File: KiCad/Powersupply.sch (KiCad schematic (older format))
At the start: 11 parts, among them J501 TE_Connectivity_282834-3, J502 CONN_01X03_FEMALE, U501 LM1086-5V, U502 LM1086-3.3V

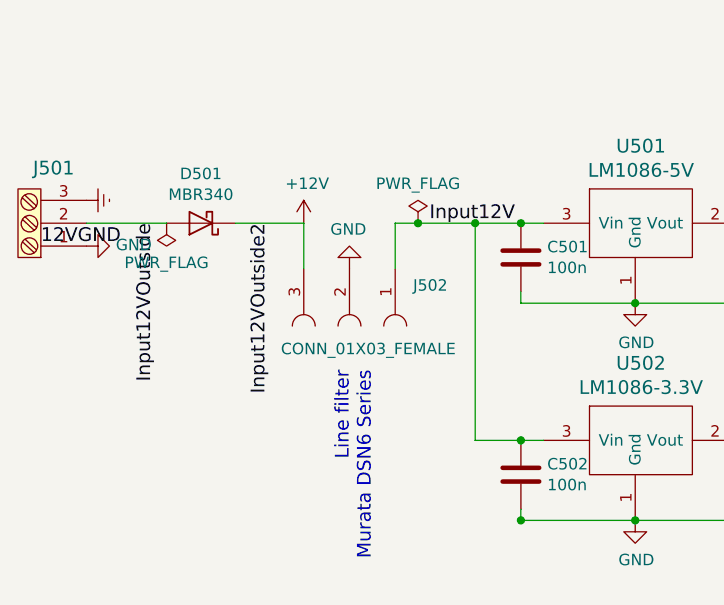
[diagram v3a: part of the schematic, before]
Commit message: Halfway through routing - need better layout to prevent rats nest
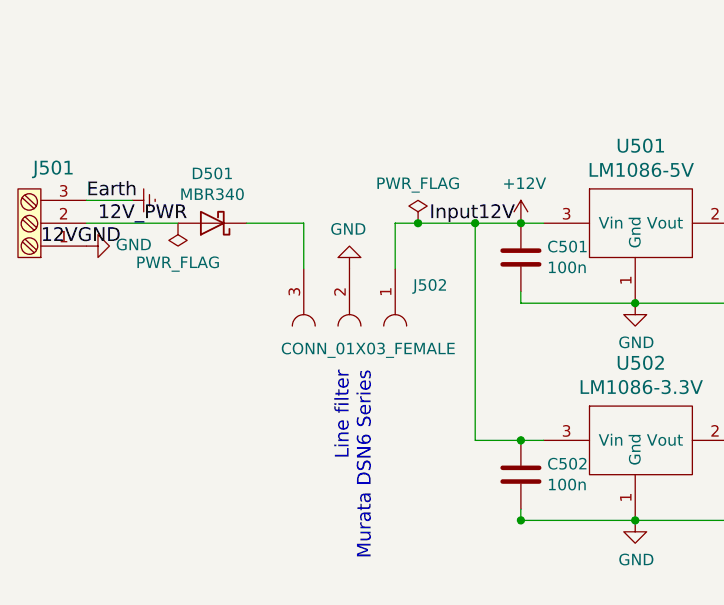
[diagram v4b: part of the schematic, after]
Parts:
- C505, C506: footprint Capacitors_THT:CP_Radial_D7.5mm_P2.50mm -> Capacitors_THT:CP_Radial_D6.3mm_P2.50mm
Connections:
- net labels added: 12V_PWR
- net labels removed: Input12VOutside, Input12VOutside2
- wire segments 27 -> 28
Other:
- moved on the sheet: D501
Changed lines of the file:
@@
 POWER3V3
 $Comp
-L +3V3 #PWR0104
+L +3V3 #PWR0112
 U 1 1 592AD7CB
 P 2200 1500
-F 0 "#PWR0104" H 2200 1350 50  0001 C CNN
+F 0 "#PWR0112" H 2200 1350 50  0001 C CNN
 F 1 "+3V3" V 2215 1628 50  0000 L CNN
 F 2 "" H 2200 1500 50  0001 C CNN
@@
 	2100 1500 2200 1500
 $Comp
-L PWR_FLAG #FLG0105
+L PWR_FLAG #FLG0113
 U 1 1 592B4E13
 P 2850 1450
-F 0 "#FLG0105" H 2850 1525 50  0001 C CNN
+F 0 "#FLG0113" H 2850 1525 50  0001 C CNN
 F 1 "PWR_FLAG" H 2850 1624 50  0000 C CNN
 F 2 "" H 2850 1450 50  0001 C CNN
@@
 $EndComp
 $Comp
-L GND #PWR0106
+L GND #PWR0114
 U 1 1 592B4E96
 P 2850 1450
-F 0 "#PWR0106" H 2850 1200 50  0001 C CNN
+F 0 "#PWR0114" H 2850 1200 50  0001 C CNN
 F 1 "GND" H 2855 1277 50  0000 C CNN
 F 2 "" H 2850 1450 50  0001 C CNN
@@
 $EndComp
 $Comp
-L GND #PWR0107
+L GND #PWR0115
 U 1 1 5924C039
 P 3350 4250
-F 0 "#PWR0107" H 3350 4000 50  0001 C CNN
+F 0 "#PWR0115" H 3350 4000 50  0001 C CNN
 F 1 "GND" H 3355 4077 50  0000 C CNN
 F 2 "" H 3350 4250 50  0001 C CNN
@@
 F 0 "C506" H 4768 4096 50  0000 L CNN
 F 1 "100uF" H 4768 4005 50  0000 L CNN
-F 2 "Capacitors_THT:CP_Radial_D7.5mm_P2.50mm" H 4688 3900 50  0001 C CNN
-F 3 "http://se.rs-online.com/web/p/aluminium-capacitors/8650656/" H 4650 4050 50  0001 C CNN
+F 2 "Capacitors_THT:CP_Radial_D6.3mm_P2.50mm" H 4688 3900 50  0001 C CNN
+F 3 "https://www.digikey.se/product-detail/en/nichicon/ULD1C101MED1TD/493-14722-1-ND/6161730" H 4650 4050 50  0001 C CNN
 	1    4650 4050
 	1    0    0    -1
@@
 Connection ~ 4200 2950
 $Comp
-L GND #PWR0108
+L GND #PWR0116
 U 1 1 5924DE85
 P 950 3050
-F 0 "#PWR0108" H 950 2800 50  0001 C CNN
+F 0 "#PWR0116" H 950 2800 50  0001 C CNN
 F 1 "GND" V 955 2922 50  0000 R CNN
 F 2 "" H 950 3050 50  0001 C CNN
@@
 $EndComp
 $Comp
-L PWR_FLAG #FLG0109
+L PWR_FLAG #FLG0117
 U 1 1 5924DE8B
-P 1300 2950
-F 0 "#FLG0109" H 1300 3025 50  0001 C CNN
-F 1 "PWR_FLAG" H 1300 3123 50  0000 C CNN
-F 2 "" H 1300 2950 50  0001 C CNN
-F 3 "" H 1300 2950 50  0001 C CNN
-	1    1300 2950
+P 1350 2950
+F 0 "#FLG0117" H 1350 3025 50  0001 C CNN
+F 1 "PWR_FLAG" H 1350 3123 50  0000 C CNN
+F 2 "" H 1350 2950 50  0001 C CNN
+F 3 "" H 1350 2950 50  0001 C CNN
+	1    1350 2950
 	-1   0    0    1
 $EndComp
@@
 	2050 1850 2200 1850
 $Comp
-L +5V #PWR0110
+L +5V #PWR0118
 U 1 1 5924EF19
 P 2200 1850
-F 0 "#PWR0110" H 2200 1700 50  0001 C CNN
+F 0 "#PWR0118" H 2200 1700 50  0001 C CNN
 F 1 "+5V" V 2215 1978 50  0000 L CNN
 F 2 "" H 2200 1850 50  0001 C CNN
@@
 F 0 "C505" H 4768 3146 50  0000 L CNN
 F 1 "100uF" H 4768 3055 50  0000 L CNN
-F 2 "Capacitors_THT:CP_Radial_D7.5mm_P2.50mm" H 4688 2950 50  0001 C CNN
-F 3 "http://se.rs-online.com/web/p/aluminium-capacitors/8650656/" H 4650 3100 50  0001 C CNN
+F 2 "Capacitors_THT:CP_Radial_D6.3mm_P2.50mm" H 4688 2950 50  0001 C CNN
+F 3 "https://www.digikey.se/product-detail/en/nichicon/ULD1C101MED1TD/493-14722-1-ND/6161730" H 4650 3100 50  0001 C CNN
 	1    4650 3100
 	1    0    0    -1
@@
 $EndComp
 $Comp
-L GND #PWR0111
+L GND #PWR0119
 U 1 1 5924DE5E
 P 3350 3300
-F 0 "#PWR0111" H 3350 3050 50  0001 C CNN
+F 0 "#PWR0119" H 3350 3050 50  0001 C CNN
 F 1 "GND" H 3355 3127 50  0000 C CNN
 F 2 "" H 3350 3300 50  0001 C CNN
@@
 L MBR340 D501
 U 1 1 5928EED5
-P 1450 2950
-F 0 "D501" H 1450 2734 50  0000 C CNN
-F 1 "MBR340" H 1450 2825 50  0000 C CNN
-F 2 "Diodes_SMD:D_SMB" H 1450 2775 50  0001 C CNN
-F 3 "" H 1450 2950 50  0001 C CNN
-	1    1450 2950
-	-1   0    0    1
-$EndComp
-Text Label 1250 2950 3    60   ~ 0
-Input12VOutside
-Wire Wire Line
-	950  2950 1300 2950
+P 1500 2950
+F 0 "D501" H 1500 2734 50  0000 C CNN
+F 1 "MBR340" H 1500 2825 50  0000 C CNN
+F 2 "Diodes_SMD:D_SMB" H 1500 2775 50  0001 C CNN
+F 3 "" H 1500 2950 50  0001 C CNN
+	1    1500 2950
+	-1   0    0    1
+$EndComp
+Wire Wire Line
+	950  2950 1350 2950
 $Comp
 L CONN_01X03_FEMALE J502
@@
 $EndComp
 $Comp
-L GND #PWR0112
+L GND #PWR0120
 U 1 1 592909E6
 P 2100 3150
-F 0 "#PWR0112" H 2100 2900 50  0001 C CNN
+F 0 "#PWR0120" H 2100 2900 50  0001 C CNN
 F 1 "GND" H 2105 2977 50  0000 C CNN
 F 2 "" H 2100 3150 50  0001 C CNN
@@
 	-1   0    0    1
 $EndComp
-Text Label 1750 2950 3    60   ~ 0
-Input12VOutside2
-Wire Wire Line
-	1600 2950 1900 2950
+Wire Wire Line
+	1650 2950 1900 2950
 Wire Wire Line
 	1900 2950 1900 3150
 $Comp
-L +12V #PWR0113
+L +12V #PWR0121
 U 1 1 592CA1C3
-P 1900 2950
-F 0 "#PWR0113" H 1900 2800 50  0001 C CNN
-F 1 "+12V" H 1915 3123 50  0000 C CNN
-F 2 "" H 1900 2950 50  0001 C CNN
-F 3 "" H 1900 2950 50  0001 C CNN
-	1    1900 2950
+P 2850 2950
+F 0 "#PWR0121" H 2850 2800 50  0001 C CNN
+F 1 "+12V" H 2865 3123 50  0000 C CNN
+F 2 "" H 2850 2950 50  0001 C CNN
+F 3 "" H 2850 2950 50  0001 C CNN
+	1    2850 2950
 	1    0    0    -1
 $EndComp
@@
 Connection ~ 4200 4250
 $Comp
-L PWR_FLAG #FLG0114
+L PWR_FLAG #FLG0122
 U 1 1 592E87DD
 P 3450 1450
-F 0 "#FLG0114" H 3450 1525 50  0001 C CNN
+F 0 "#FLG0122" H 3450 1525 50  0001 C CNN
 F 1 "PWR_FLAG" H 3450 1623 50  0000 C CNN
 F 2 "" H 3450 1450 50  0001 C CNN
@@
 $EndComp
 $Comp
-L +12V #PWR0115
+L +12V #PWR0123
 U 1 1 592E8840
 P 3450 1450
-F 0 "#PWR0115" H 3450 1300 50  0001 C CNN
+F 0 "#PWR0123" H 3450 1300 50  0001 C CNN
 F 1 "+12V" H 3465 1623 50  0000 C CNN
 F 2 "" H 3450 1450 50  0001 C CNN
@@
 $EndComp
 $Comp
-L PWR_FLAG #FLG0116
+L PWR_FLAG #FLG0124
 U 1 1 592EF7D9
 P 2400 2950
-F 0 "#FLG0116" H 2400 3025 50  0001 C CNN
+F 0 "#FLG0124" H 2400 3025 50  0001 C CNN
 F 1 "PWR_FLAG" H 2400 3123 50  0000 C CNN
 F 2 "" H 2400 2950 50  0001 C CNN
@@
 Connection ~ 2400 2950
 $Comp
-L Earth #PWR0117
+L Earth #PWR0125
 U 1 1 5933481E
-P 950 2850
-F 0 "#PWR0117" H 950 2600 50  0001 C CNN
-F 1 "Earth" H 950 2700 50  0001 C CNN
-F 2 "" H 950 2850 50  0001 C CNN
-F 3 "" H 950 2850 50  0001 C CNN
-	1    950  2850
+P 1150 2850
+F 0 "#PWR0125" H 1150 2600 50  0001 C CNN
+F 1 "Earth" H 1150 2700 50  0001 C CNN
+F 2 "" H 1150 2850 50  0001 C CNN
+F 3 "" H 1150 2850 50  0001 C CNN
+	1    1150 2850
 	0    -1   -1   0
 $EndComp
@@
 $EndComp
 $Comp
-L Earth #PWR0118
+L Earth #PWR0126
 U 1 1 59344C28
 P 3150 1500
-F 0 "#PWR0118" H 3150 1250 50  0001 C CNN
+F 0 "#PWR0126" H 3150 1250 50  0001 C CNN
 F 1 "Earth" H 3150 1350 50  0001 C CNN
 F 2 "" H 3150 1500 50  0001 C CNN
@@
 Wire Wire Line
 	3150 1450 2850 1450
+Wire Wire Line
+	950  2850 1150 2850
+Text Label 950  2850 0    60   ~ 0
+Earth
+Text Label 1000 2950 0    60   ~ 0
+12V_PWR
 $EndSCHEMATC

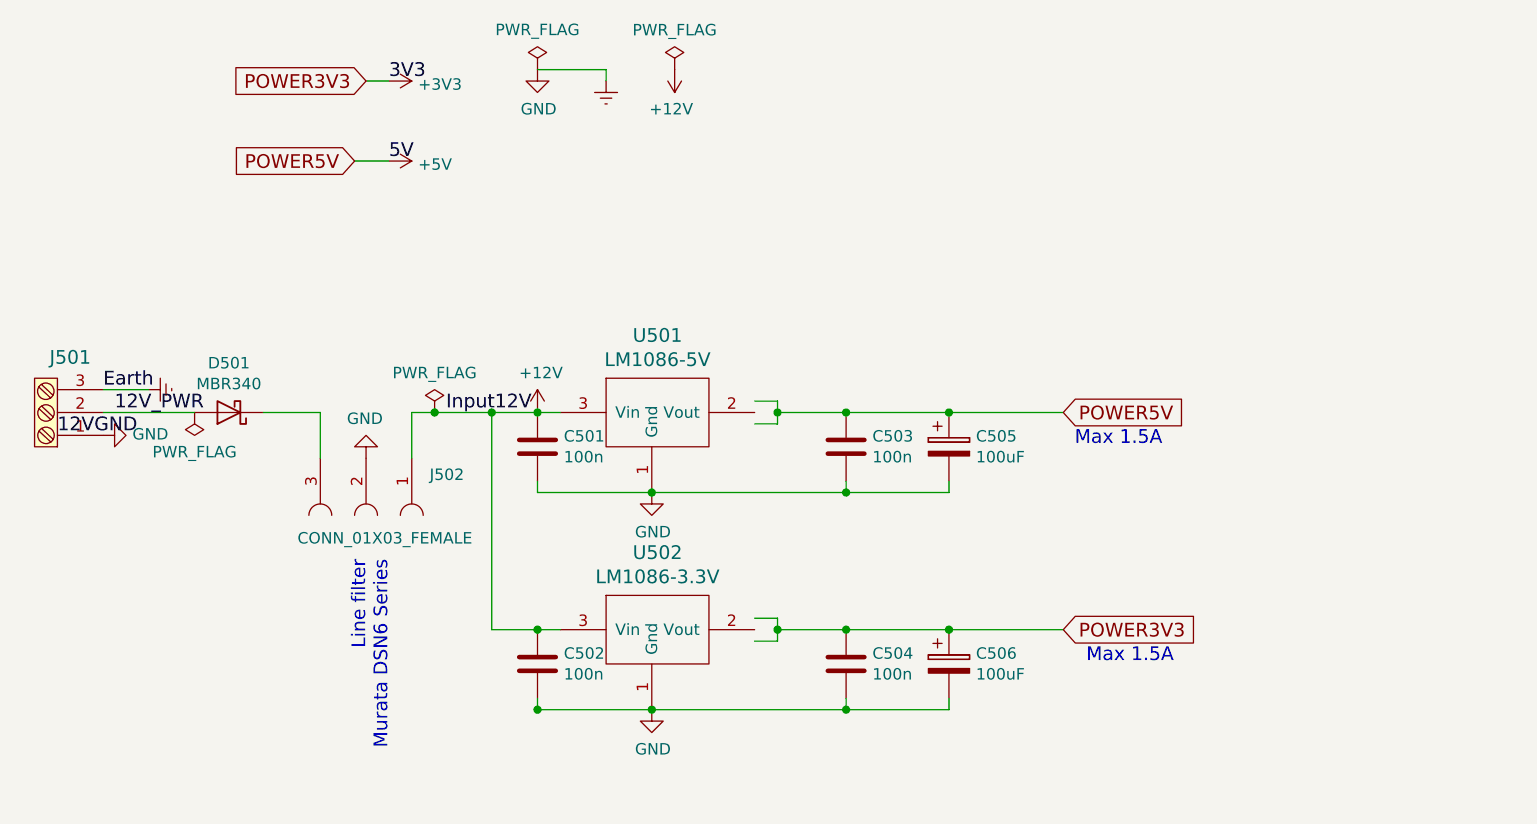
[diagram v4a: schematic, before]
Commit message: New sense input circuits. New layout
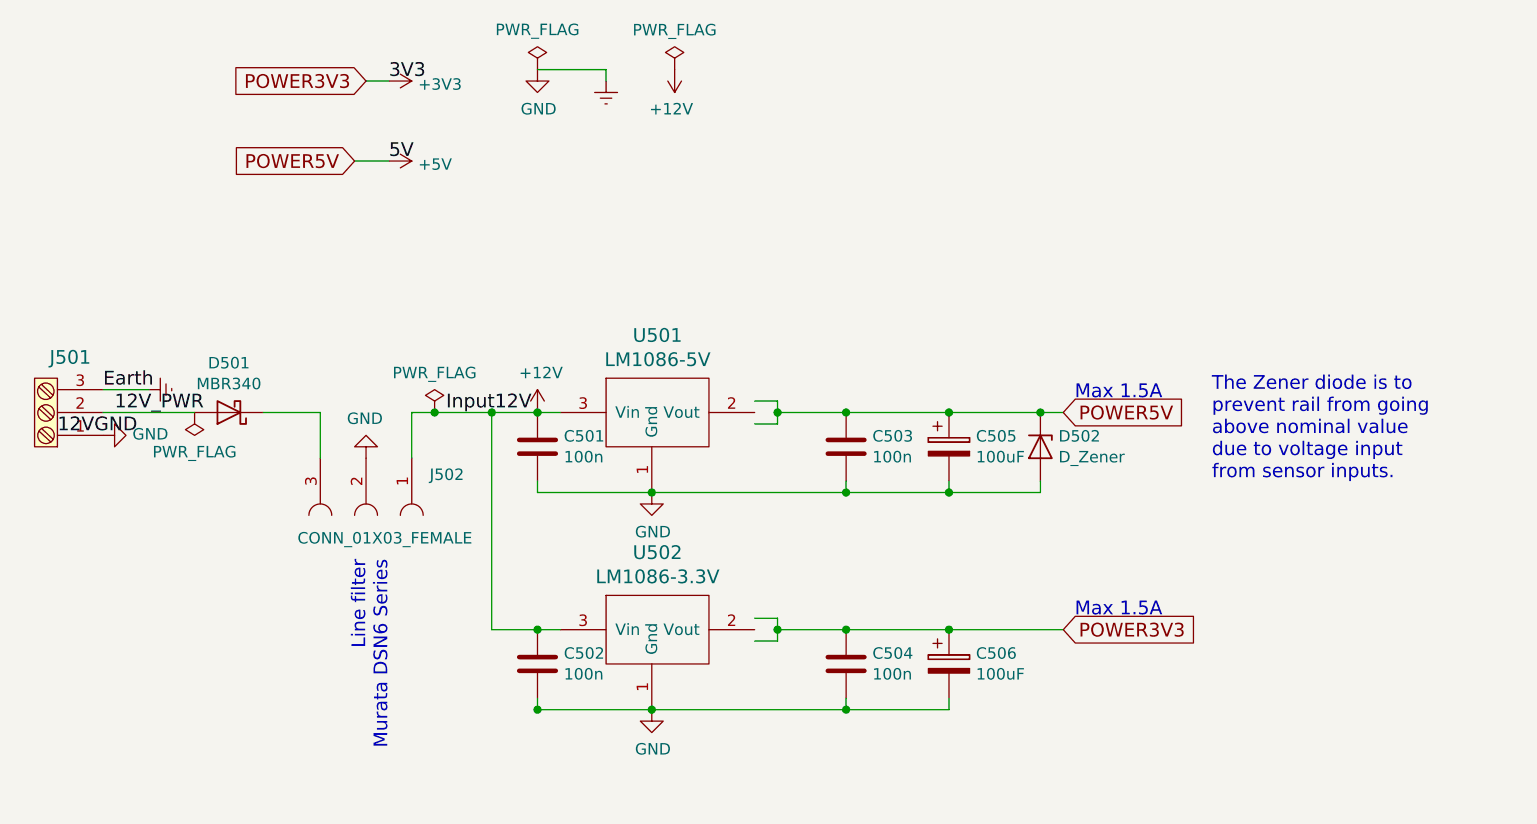
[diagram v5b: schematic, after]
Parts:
- added D502: D_Zener, Diodes_SMD:D_SOD-123, symbol D_Zener
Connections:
- wire segments 28 -> 29
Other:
- note added: "The Zener diode is to\nprevent rail from going\nabove nominal value\ndue to voltage input\nfrom sensor inputs."
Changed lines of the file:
@@
 POWER3V3
 $Comp
-L +3V3 #PWR0112
+L +3V3 #PWR0120
 U 1 1 592AD7CB
 P 2200 1500
-F 0 "#PWR0112" H 2200 1350 50  0001 C CNN
+F 0 "#PWR0120" H 2200 1350 50  0001 C CNN
 F 1 "+3V3" V 2215 1628 50  0000 L CNN
 F 2 "" H 2200 1500 50  0001 C CNN
@@
 	2100 1500 2200 1500
 $Comp
-L PWR_FLAG #FLG0113
+L PWR_FLAG #FLG0121
 U 1 1 592B4E13
 P 2850 1450
-F 0 "#FLG0113" H 2850 1525 50  0001 C CNN
+F 0 "#FLG0121" H 2850 1525 50  0001 C CNN
 F 1 "PWR_FLAG" H 2850 1624 50  0000 C CNN
 F 2 "" H 2850 1450 50  0001 C CNN
@@
 $EndComp
 $Comp
-L GND #PWR0114
+L GND #PWR0122
 U 1 1 592B4E96
 P 2850 1450
-F 0 "#PWR0114" H 2850 1200 50  0001 C CNN
+F 0 "#PWR0122" H 2850 1200 50  0001 C CNN
 F 1 "GND" H 2855 1277 50  0000 C CNN
 F 2 "" H 2850 1450 50  0001 C CNN
@@
 $EndComp
 $Comp
-L GND #PWR0115
+L GND #PWR0123
 U 1 1 5924C039
 P 3350 4250
-F 0 "#PWR0115" H 3350 4000 50  0001 C CNN
+F 0 "#PWR0123" H 3350 4000 50  0001 C CNN
 F 1 "GND" H 3355 4077 50  0000 C CNN
 F 2 "" H 3350 4250 50  0001 C CNN
@@
 Connection ~ 4200 2950
 $Comp
-L GND #PWR0116
+L GND #PWR0124
 U 1 1 5924DE85
 P 950 3050
-F 0 "#PWR0116" H 950 2800 50  0001 C CNN
+F 0 "#PWR0124" H 950 2800 50  0001 C CNN
 F 1 "GND" V 955 2922 50  0000 R CNN
 F 2 "" H 950 3050 50  0001 C CNN
@@
 $EndComp
 $Comp
-L PWR_FLAG #FLG0117
+L PWR_FLAG #FLG0125
 U 1 1 5924DE8B
 P 1350 2950
-F 0 "#FLG0117" H 1350 3025 50  0001 C CNN
+F 0 "#FLG0125" H 1350 3025 50  0001 C CNN
 F 1 "PWR_FLAG" H 1350 3123 50  0000 C CNN
 F 2 "" H 1350 2950 50  0001 C CNN
@@
 	2050 1850 2200 1850
 $Comp
-L +5V #PWR0118
+L +5V #PWR0126
 U 1 1 5924EF19
 P 2200 1850
-F 0 "#PWR0118" H 2200 1700 50  0001 C CNN
+F 0 "#PWR0126" H 2200 1700 50  0001 C CNN
 F 1 "+5V" V 2215 1978 50  0000 L CNN
 F 2 "" H 2200 1850 50  0001 C CNN
@@
 	1    0    0    -1
 $EndComp
-Text Notes 5200 3100 0    60   ~ 0
+Text Notes 5200 2900 0    60   ~ 0
 Max 1.5A
-Text Notes 5250 4050 0    60   ~ 0
+Text Notes 5200 3850 0    60   ~ 0
 Max 1.5A
 Text Label 2450 2950 0    60   ~ 0
@@
 $EndComp
 $Comp
-L GND #PWR0119
+L GND #PWR0127
 U 1 1 5924DE5E
 P 3350 3300
-F 0 "#PWR0119" H 3350 3050 50  0001 C CNN
+F 0 "#PWR0127" H 3350 3050 50  0001 C CNN
 F 1 "GND" H 3355 3127 50  0000 C CNN
 F 2 "" H 3350 3300 50  0001 C CNN
@@
 $EndComp
 Wire Wire Line
-	2850 3300 4650 3300
+	2850 3300 5050 3300
 Wire Wire Line
 	2850 3300 2850 3250
@@
 $EndComp
 $Comp
-L GND #PWR0120
+L GND #PWR0128
 U 1 1 592909E6
 P 2100 3150
-F 0 "#PWR0120" H 2100 2900 50  0001 C CNN
+F 0 "#PWR0128" H 2100 2900 50  0001 C CNN
 F 1 "GND" H 2105 2977 50  0000 C CNN
 F 2 "" H 2100 3150 50  0001 C CNN
@@
 	1900 2950 1900 3150
 $Comp
-L +12V #PWR0121
+L +12V #PWR0129
 U 1 1 592CA1C3
 P 2850 2950
-F 0 "#PWR0121" H 2850 2800 50  0001 C CNN
+F 0 "#PWR0129" H 2850 2800 50  0001 C CNN
 F 1 "+12V" H 2865 3123 50  0000 C CNN
 F 2 "" H 2850 2950 50  0001 C CNN
@@
 Connection ~ 4200 4250
 $Comp
-L PWR_FLAG #FLG0122
+L PWR_FLAG #FLG0130
 U 1 1 592E87DD
 P 3450 1450
-F 0 "#FLG0122" H 3450 1525 50  0001 C CNN
+F 0 "#FLG0130" H 3450 1525 50  0001 C CNN
 F 1 "PWR_FLAG" H 3450 1623 50  0000 C CNN
 F 2 "" H 3450 1450 50  0001 C CNN
@@
 $EndComp
 $Comp
-L +12V #PWR0123
+L +12V #PWR0131
 U 1 1 592E8840
 P 3450 1450
-F 0 "#PWR0123" H 3450 1300 50  0001 C CNN
+F 0 "#PWR0131" H 3450 1300 50  0001 C CNN
 F 1 "+12V" H 3465 1623 50  0000 C CNN
 F 2 "" H 3450 1450 50  0001 C CNN
@@
 $EndComp
 $Comp
-L PWR_FLAG #FLG0124
+L PWR_FLAG #FLG0132
 U 1 1 592EF7D9
 P 2400 2950
-F 0 "#FLG0124" H 2400 3025 50  0001 C CNN
+F 0 "#FLG0132" H 2400 3025 50  0001 C CNN
 F 1 "PWR_FLAG" H 2400 3123 50  0000 C CNN
 F 2 "" H 2400 2950 50  0001 C CNN
@@
 Connection ~ 2400 2950
 $Comp
-L Earth #PWR0125
+L Earth #PWR0133
 U 1 1 5933481E
 P 1150 2850
-F 0 "#PWR0125" H 1150 2600 50  0001 C CNN
+F 0 "#PWR0133" H 1150 2600 50  0001 C CNN
 F 1 "Earth" H 1150 2700 50  0001 C CNN
 F 2 "" H 1150 2850 50  0001 C CNN
@@
 $EndComp
 $Comp
-L Earth #PWR0126
+L Earth #PWR0134
 U 1 1 59344C28
 P 3150 1500
-F 0 "#PWR0126" H 3150 1250 50  0001 C CNN
+F 0 "#PWR0134" H 3150 1250 50  0001 C CNN
 F 1 "Earth" H 3150 1350 50  0001 C CNN
 F 2 "" H 3150 1500 50  0001 C CNN
@@
 Text Label 1000 2950 0    60   ~ 0
 12V_PWR
+$Comp
+L D_Zener D502
+U 1 1 59376489
+P 5050 3100
+F 0 "D502" V 5004 3179 50  0000 L CNN
+F 1 "D_Zener" V 5095 3179 50  0000 L CNN
+F 2 "Diodes_SMD:D_SOD-123" H 5050 3100 50  0001 C CNN
+F 3 "https://www.digikey.se/products/en?keywords=1N4733AW-TPMSCT-ND" H 5050 3100 50  0001 C CNN
+	1    5050 3100
+	0    1    1    0
+$EndComp
+Wire Wire Line
+	5050 3300 5050 3250
+Connection ~ 4650 3300
+Text Notes 5800 3250 0    60   ~ 0
+The Zener diode is to\nprevent rail from going\nabove nominal value\ndue to voltage input\nfrom sensor inputs.
+Connection ~ 5050 2950
 $EndSCHEMATC

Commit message: Routing
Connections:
- net labels added: 12V_PWR2
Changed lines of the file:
@@
 The Zener diode is to\nprevent rail from going\nabove nominal value\ndue to voltage input\nfrom sensor inputs.
 Connection ~ 5050 2950
+Text Label 1700 2950 0    60   ~ 0
+12V_PWR2
 $EndSCHEMATC

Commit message: Starting another routing pass
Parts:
- U501, U502: footprint TO_SOT_Packages_THT:TO-220_Horizontal -> TO_SOT_Packages_THT:TO-220_Vertical
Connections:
- wire segments 29 -> 23
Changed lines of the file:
@@
 	1    0    0    -1
 $EndComp
-Wire Wire Line
-	3900 3900 5150 3900
-Wire Wire Line
-	3900 3850 3900 3950
-Wire Wire Line
-	3900 3850 3800 3850
 Connection ~ 4200 3900
 Connection ~ 2850 3900
@@
 $EndComp
 Wire Wire Line
-	3900 2950 5150 2950
-Wire Wire Line
-	3900 2900 3800 2900
+	3800 2950 5150 2950
 Connection ~ 4200 2950
 $Comp
@@
 Text Label 2200 1850 0    60   ~ 0
 5V
-Connection ~ 3900 2950
 $Comp
 L C C503
@@
 Connection ~ 4200 3300
 Wire Wire Line
-	3900 3000 3800 3000
-Wire Wire Line
-	3900 2900 3900 3000
-Wire Wire Line
 	2850 4200 2850 4250
 Connection ~ 2850 4250
@@
 Wire Wire Line
 	4650 4250 4650 4200
-Wire Wire Line
-	3900 3950 3800 3950
-Connection ~ 3900 3900
 $Comp
 L LM1086-3.3V U502
@@
 F 0 "U502" H 3375 3437 60  0000 C CNN
 F 1 "LM1086-3.3V" H 3375 3331 60  0000 C CNN
-F 2 "TO_SOT_Packages_THT:TO-220_Horizontal" H 3400 3500 60  0001 C CNN
+F 2 "TO_SOT_Packages_THT:TO-220_Vertical" H 3400 3500 60  0001 C CNN
 F 3 "" H 3400 3500 60  0001 C CNN
 	1    3400 3500
@@
 F 0 "U501" H 3375 2487 60  0000 C CNN
 F 1 "LM1086-5V" H 3375 2381 60  0000 C CNN
-F 2 "TO_SOT_Packages_THT:TO-220_Horizontal" H 3400 2550 60  0001 C CNN
+F 2 "TO_SOT_Packages_THT:TO-220_Vertical" H 3400 2550 60  0001 C CNN
 F 3 "" H 3400 2550 60  0001 C CNN
 	1    3400 2550
@@
 $Comp
 L PWR_FLAG #FLG0130
-U 1 1 592E87DD
-P 3450 1450
-F 0 "#FLG0130" H 3450 1525 50  0001 C CNN
-F 1 "PWR_FLAG" H 3450 1623 50  0000 C CNN
-F 2 "" H 3450 1450 50  0001 C CNN
-F 3 "" H 3450 1450 50  0001 C CNN
-	1    3450 1450
-	1    0    0    -1
-$EndComp
-$Comp
-L +12V #PWR0131
-U 1 1 592E8840
-P 3450 1450
-F 0 "#PWR0131" H 3450 1300 50  0001 C CNN
-F 1 "+12V" H 3465 1623 50  0000 C CNN
-F 2 "" H 3450 1450 50  0001 C CNN
-F 3 "" H 3450 1450 50  0001 C CNN
-	1    3450 1450
-	-1   0    0    1
-$EndComp
-$Comp
-L PWR_FLAG #FLG0132
 U 1 1 592EF7D9
 P 2400 2950
-F 0 "#FLG0132" H 2400 3025 50  0001 C CNN
+F 0 "#FLG0130" H 2400 3025 50  0001 C CNN
 F 1 "PWR_FLAG" H 2400 3123 50  0000 C CNN
 F 2 "" H 2400 2950 50  0001 C CNN
@@
 Connection ~ 2400 2950
 $Comp
-L Earth #PWR0133
+L Earth #PWR0131
 U 1 1 5933481E
 P 1150 2850
-F 0 "#PWR0133" H 1150 2600 50  0001 C CNN
+F 0 "#PWR0131" H 1150 2600 50  0001 C CNN
 F 1 "Earth" H 1150 2700 50  0001 C CNN
 F 2 "" H 1150 2850 50  0001 C CNN
@@
 $EndComp
 $Comp
-L Earth #PWR0134
+L Earth #PWR0132
 U 1 1 59344C28
 P 3150 1500
-F 0 "#PWR0134" H 3150 1250 50  0001 C CNN
+F 0 "#PWR0132" H 3150 1250 50  0001 C CNN
 F 1 "Earth" H 3150 1350 50  0001 C CNN
 F 2 "" H 3150 1500 50  0001 C CNN
@@
 Text Label 1700 2950 0    60   ~ 0
 12V_PWR2
+Wire Wire Line
+	3800 3900 5150 3900
 $EndSCHEMATC
